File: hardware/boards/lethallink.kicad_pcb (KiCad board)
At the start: 6 copper layers, 86 x 111.1 mm, 177 parts, among them J1 PCIe-x4, J2 USB3_Micro_B_Amphenol, J3 Conn_02x05_Odd_Even, J4 Conn_02x04_Odd_Even, J5 Conn_02x04_Odd_Even, Q1 Q_NMOS_GSD, Q2 Q_NMOS_GSD, Q3 Q_NMOS_GSD, Q4 Q_NMOS_GSD, Q5 SI7232DN-T1-GE3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

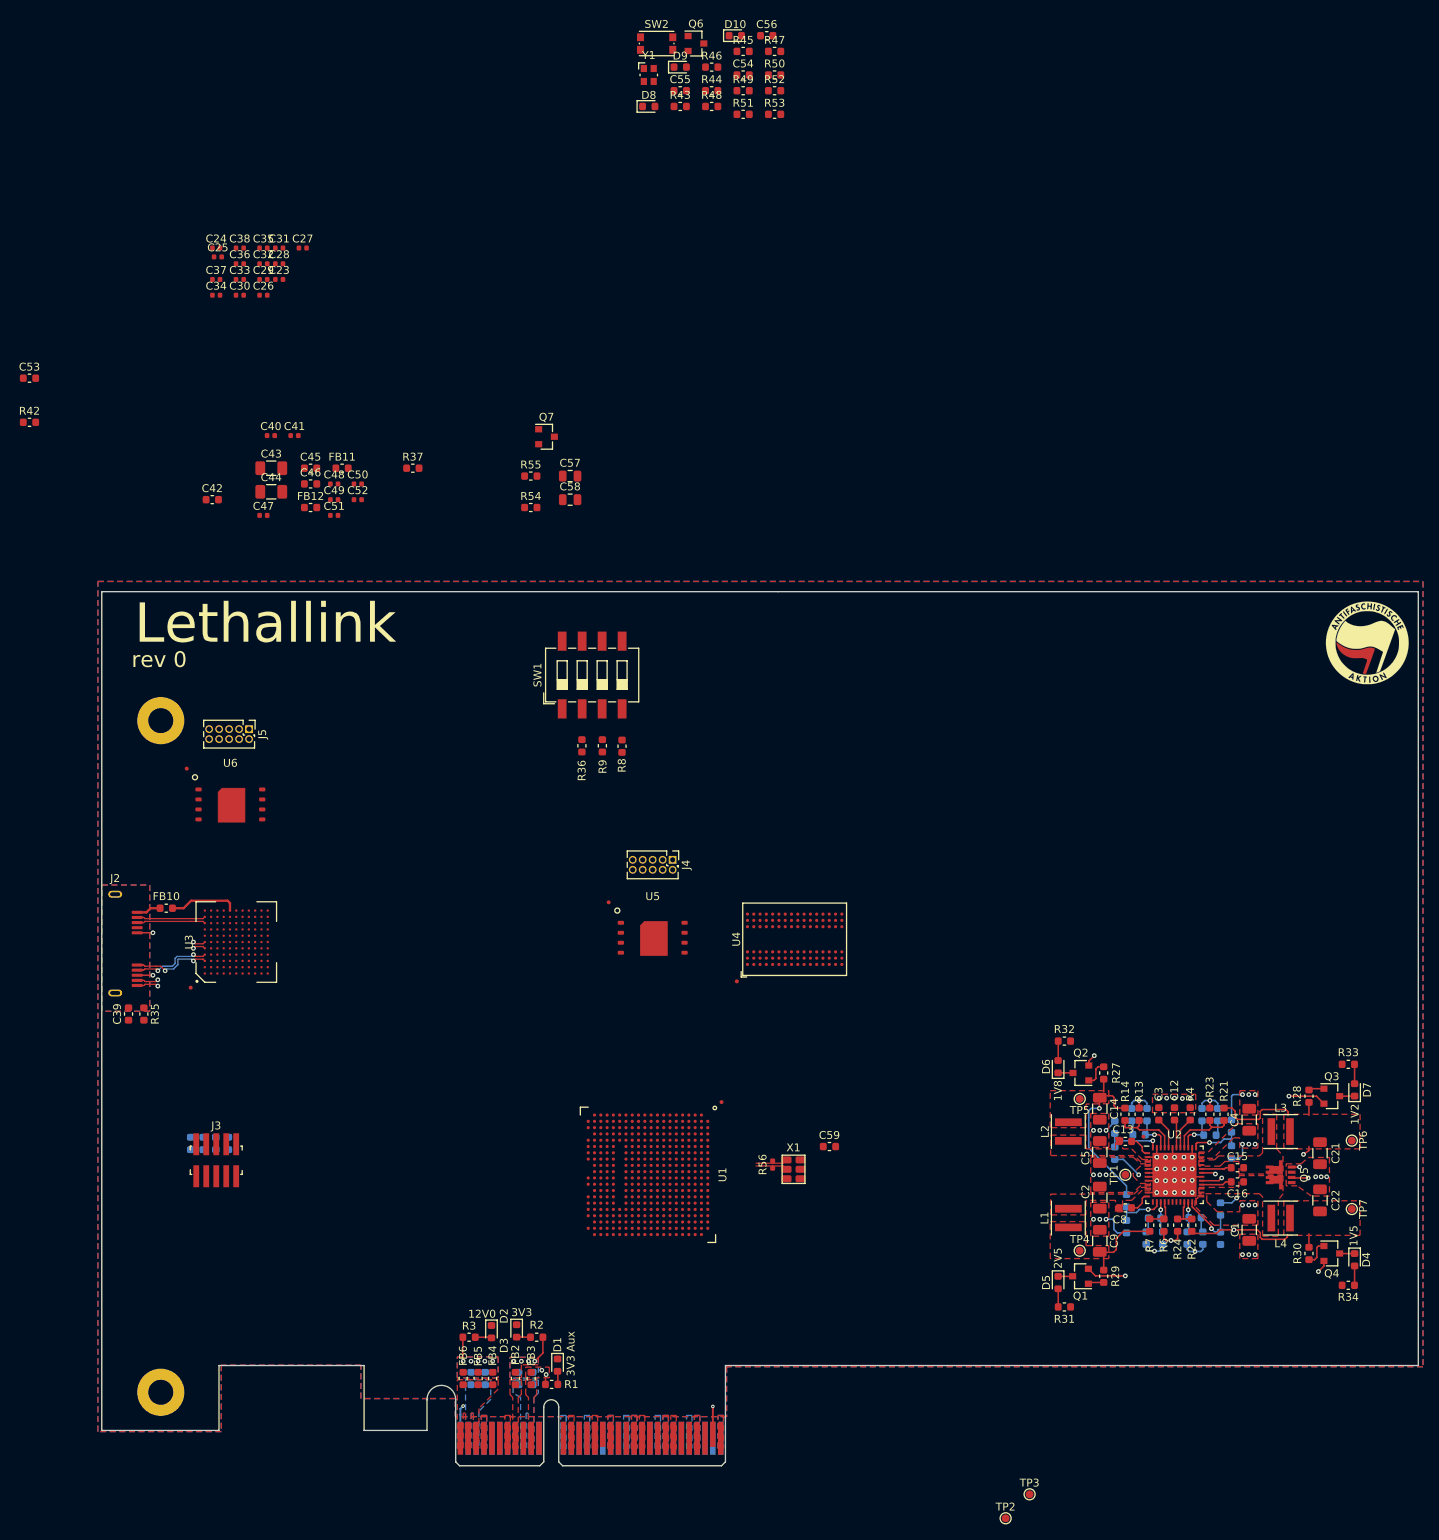
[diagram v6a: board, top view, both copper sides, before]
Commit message: Moved the power supply around and poked some of the IC lables
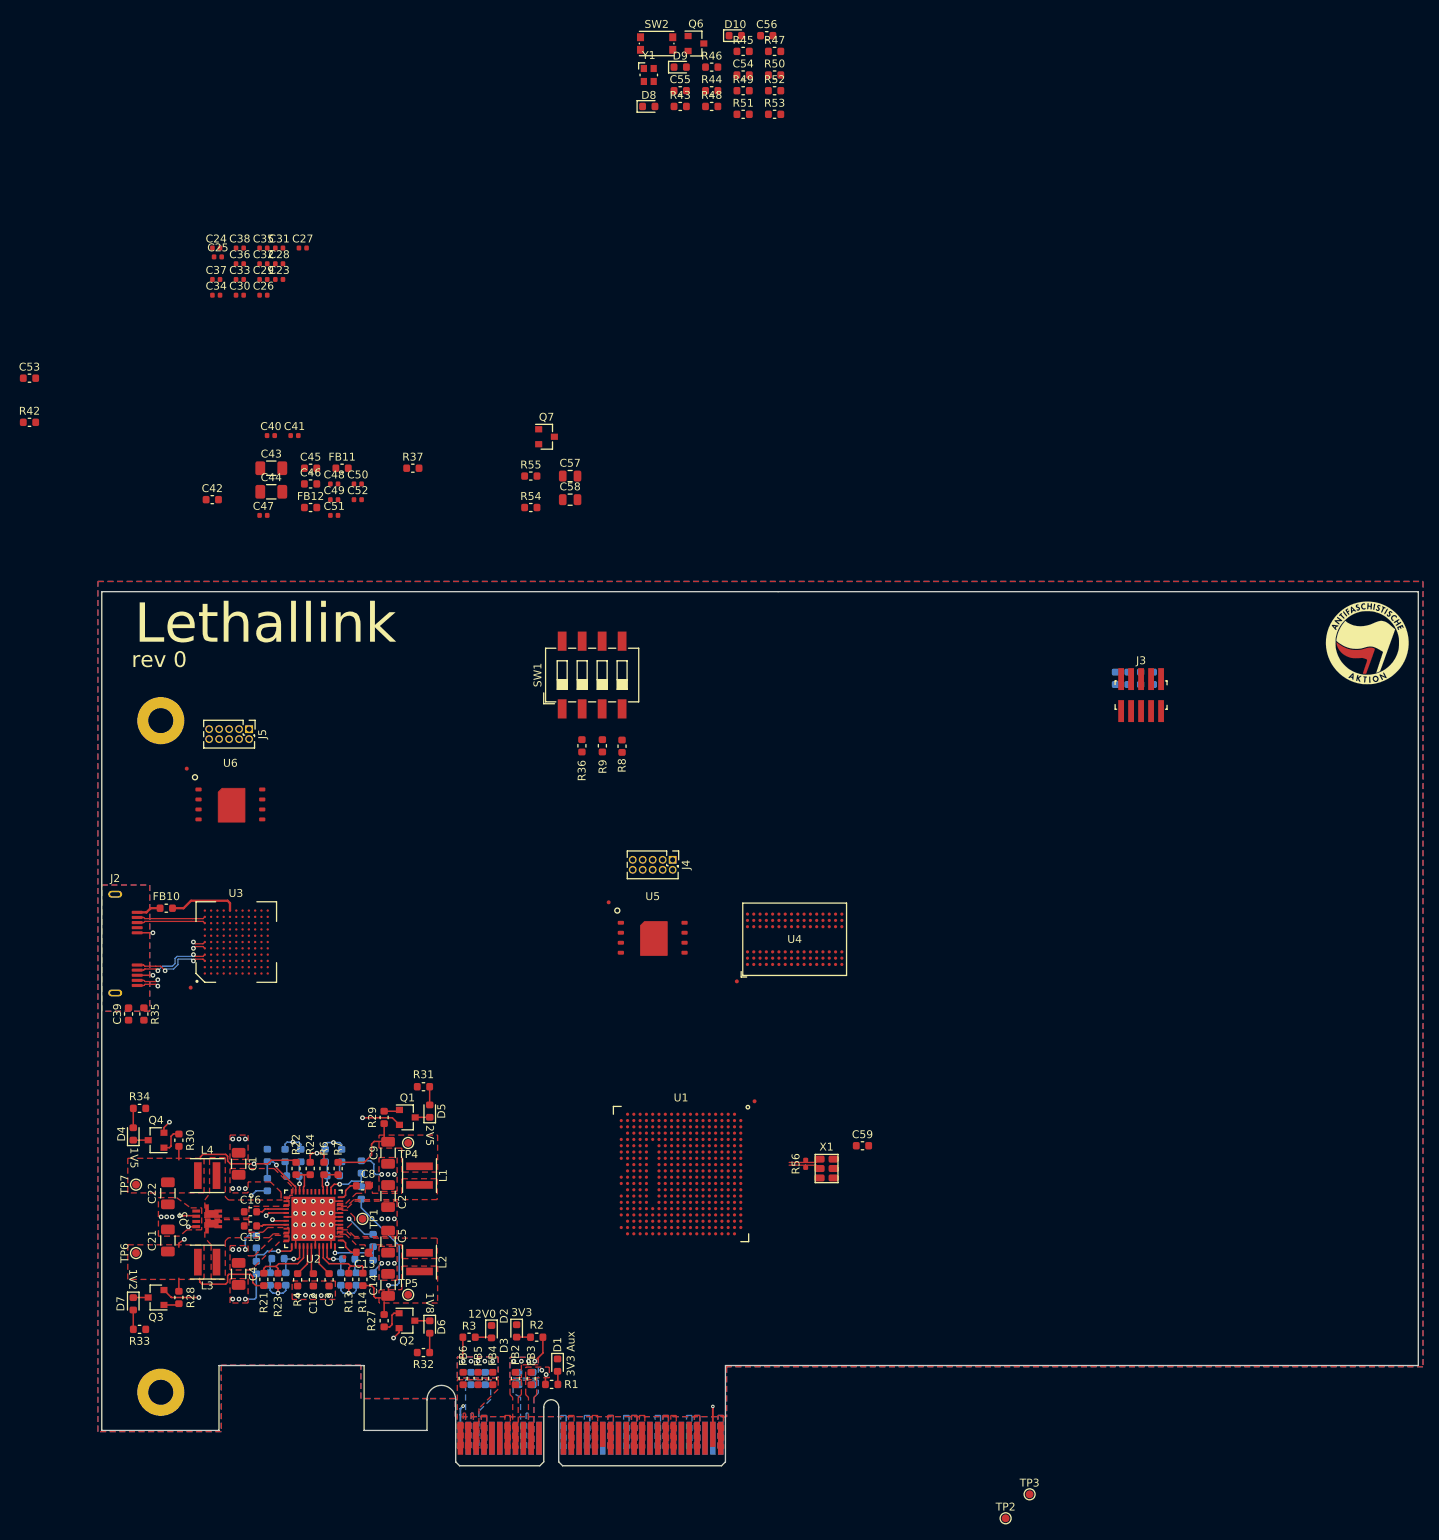
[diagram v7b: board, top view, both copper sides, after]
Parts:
- moved D7 157.7 mm to (21.4, 106.2), turned to 270 degrees
- moved R33 157.4 mm to (22.2, 109.5), turned to 180 degrees
- moved D4 156.1 mm to (21.4, 84.7), turned to 90 degrees
- moved R34 155.3 mm to (22.2, 81.4), turned to 180 degrees
- moved TP6 155.3 mm to (21.8, 99.8), turned to 90 degrees
- moved TP7 154.6 mm to (21.8, 91.1), turned to 90 degrees
- moved Q3 151.7 mm to (24.4, 105.5), turned to 180 degrees
- moved Q4 150.2 mm to (24.4, 85.5), turned to 180 degrees
- moved C21 146.9 mm to (25.9, 98.2), turned to 90 degrees
- moved C22 146.5 mm to (25.9, 92.2), turned to 270 degrees
- moved R28 146.0 mm to (27.2, 105.5), turned to 270 degrees
- moved R30 144.4 mm to (27.2, 85.5), turned to 90 degrees
- moved L3 137.5 mm to (30.9, 101.0), turned to 180 degrees
- moved Q5 136.6 mm to (30.9, 95.5), turned to 0 degrees
- moved L4 136.6 mm to (30.9, 90.0), turned to 180 degrees
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
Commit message: Added a clock fanout buffer for the PCIe REFCLOCK to connect to the FPGAs SERDES banks
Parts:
- added C60: 0.1uF, Capacitor_SMD:C_0603_1608Metric, F.Cu at (115.8, 120.3)
- added C61: 0.1uF, Capacitor_SMD:C_0603_1608Metric, F.Cu at (115.8, 123.4)
- added R57: 1k, Resistor_SMD:R_0603_1608Metric, F.Cu at (115.8, 126.4)
- added U7: SI5330B, Package_DFN_QFN:VQFN-24-1EP_4x4mm_P0.5mm_EP2.45x2.45mm, F.Cu at (110.8, 123.4)
